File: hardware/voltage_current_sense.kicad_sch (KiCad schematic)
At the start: 36 parts, among them U10 NME0505SC, U11 LM324, U6 INA126U/2K5, U8 LTC6992CS6-2-TRMPBF, U9 6N137

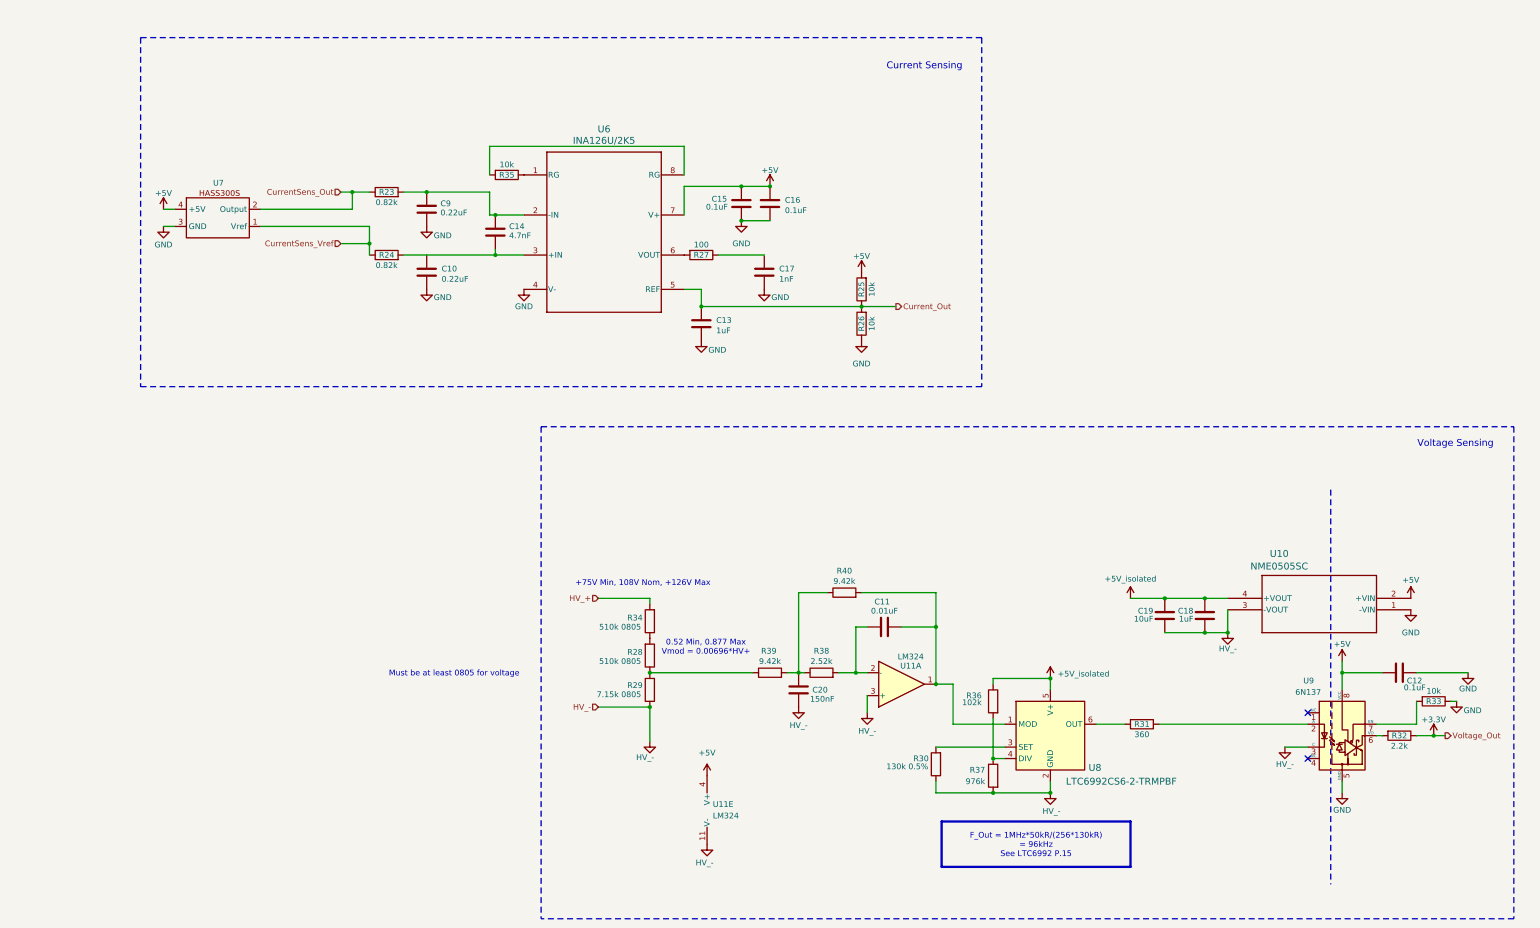
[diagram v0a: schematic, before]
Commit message: changes to sensing and footprints added
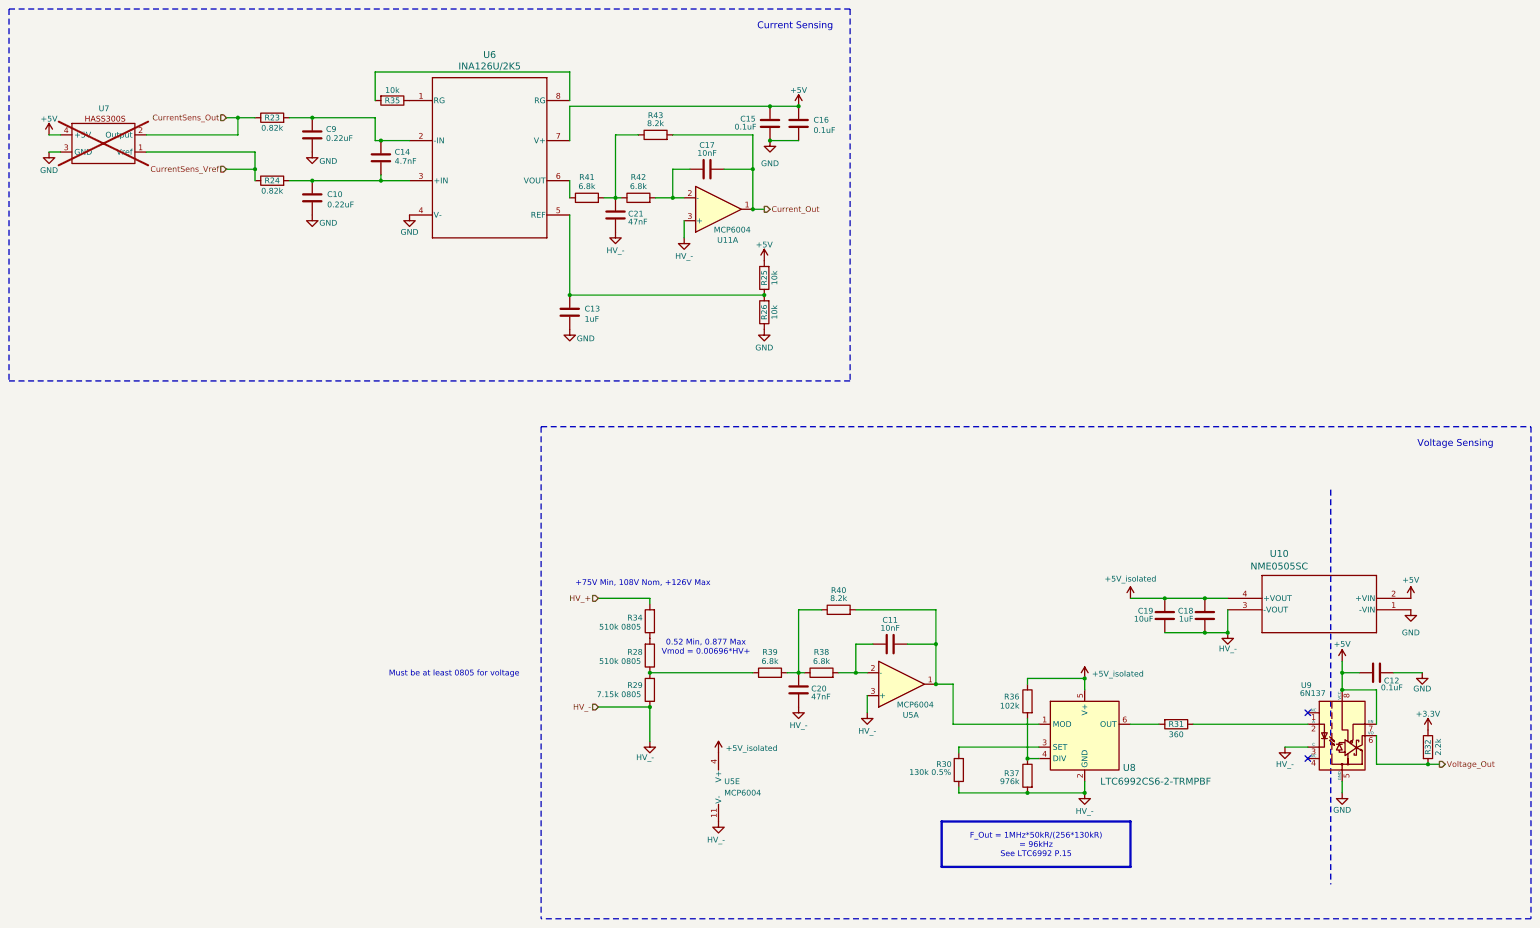
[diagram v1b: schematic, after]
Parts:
- removed R27: 100, symbol Device:R
- removed R33: 10k, symbol Device:R
- removed U11: LM324, symbol Amplifier_Operational:LM324
- added C21: 47nF, Capacitor_SMD:C_0805_2012Metric_Pad1.18x1.45mm_HandSolder, symbol Device:C
- added R41, R42: 6.8k, Resistor_SMD:R_0805_2012Metric_Pad1.20x1.40mm_HandSolder, symbol Device:R
- added R43: 8.2k, Resistor_SMD:R_0805_2012Metric_Pad1.20x1.40mm_HandSolder, symbol Device:R
- added U11, U5: MCP6004, Package_SO:SOIC-14_3.9x8.7mm_P1.27mm, symbol Amplifier_Operational:MCP6004
- C10, C12, C13, C14, C15, C16, C18, C19, C9: footprint (none) -> Capacitor_SMD:C_0805_2012Metric_Pad1.18x1.45mm_HandSolder
- C11: value 0.01uF -> 10nF; footprint (none) -> Capacitor_SMD:C_0805_2012Metric_Pad1.18x1.45mm_HandSolder
- C17: value 1nF -> 10nF; footprint (none) -> Capacitor_SMD:C_0805_2012Metric_Pad1.18x1.45mm_HandSolder
- C20: value 150nF -> 47nF; footprint (none) -> Capacitor_SMD:C_0805_2012Metric_Pad1.18x1.45mm_HandSolder
- R23, R24, R25, R26, R28, R29, R30, R31, R32, R34, R35, R36, R37: footprint (none) -> Resistor_SMD:R_0805_2012Metric_Pad1.20x1.40mm_HandSolder
- R38: value 2.52k -> 6.8k; footprint (none) -> Resistor_SMD:R_0805_2012Metric_Pad1.20x1.40mm_HandSolder
- R39: value 9.42k -> 6.8k; footprint (none) -> Resistor_SMD:R_0805_2012Metric_Pad1.20x1.40mm_HandSolder
- R40: value 9.42k -> 8.2k; footprint (none) -> Resistor_SMD:R_0805_2012Metric_Pad1.20x1.40mm_HandSolder
- U6: footprint D0008A_N -> Package_SO:SOIC-8_5.3x6.2mm_P1.27mm
- U7: now not fitted
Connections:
- net +5V: now also U9.7 (EN)
- net +5V_isolated: now also U5.4 (V+)
- net Current_Out: now also C17.2, R43.2, U11.1; no longer C13.1, R25.1, R26.2, U6.5 (REF)
- net GND: no longer C17.2
- net HV_-: now also C21.1, U11.3 (+), U5.11 (V-), U5.3 (+)
- net at C11.2, R40.2, U8.1 (MOD): now also U5.1
- net at C17.1: now also R42.2, U11.2 (-)
- net Voltage_Out: now reaches R32.2, U9.6 (VO)
- net at U6.6 (VOUT): now also R41.1
- net at C11.1, R38.2: now also U5.2 (-)
- new net: C21.2, R41.2, R42.1, R43.1
- new net: C13.1, R25.1, R26.2, U6.5 (REF)
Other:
- moved on the sheet: C10, C11, C12, C13, C14, C15, C16, C9, R23, R24, R25, R26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

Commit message: completed main board schematic
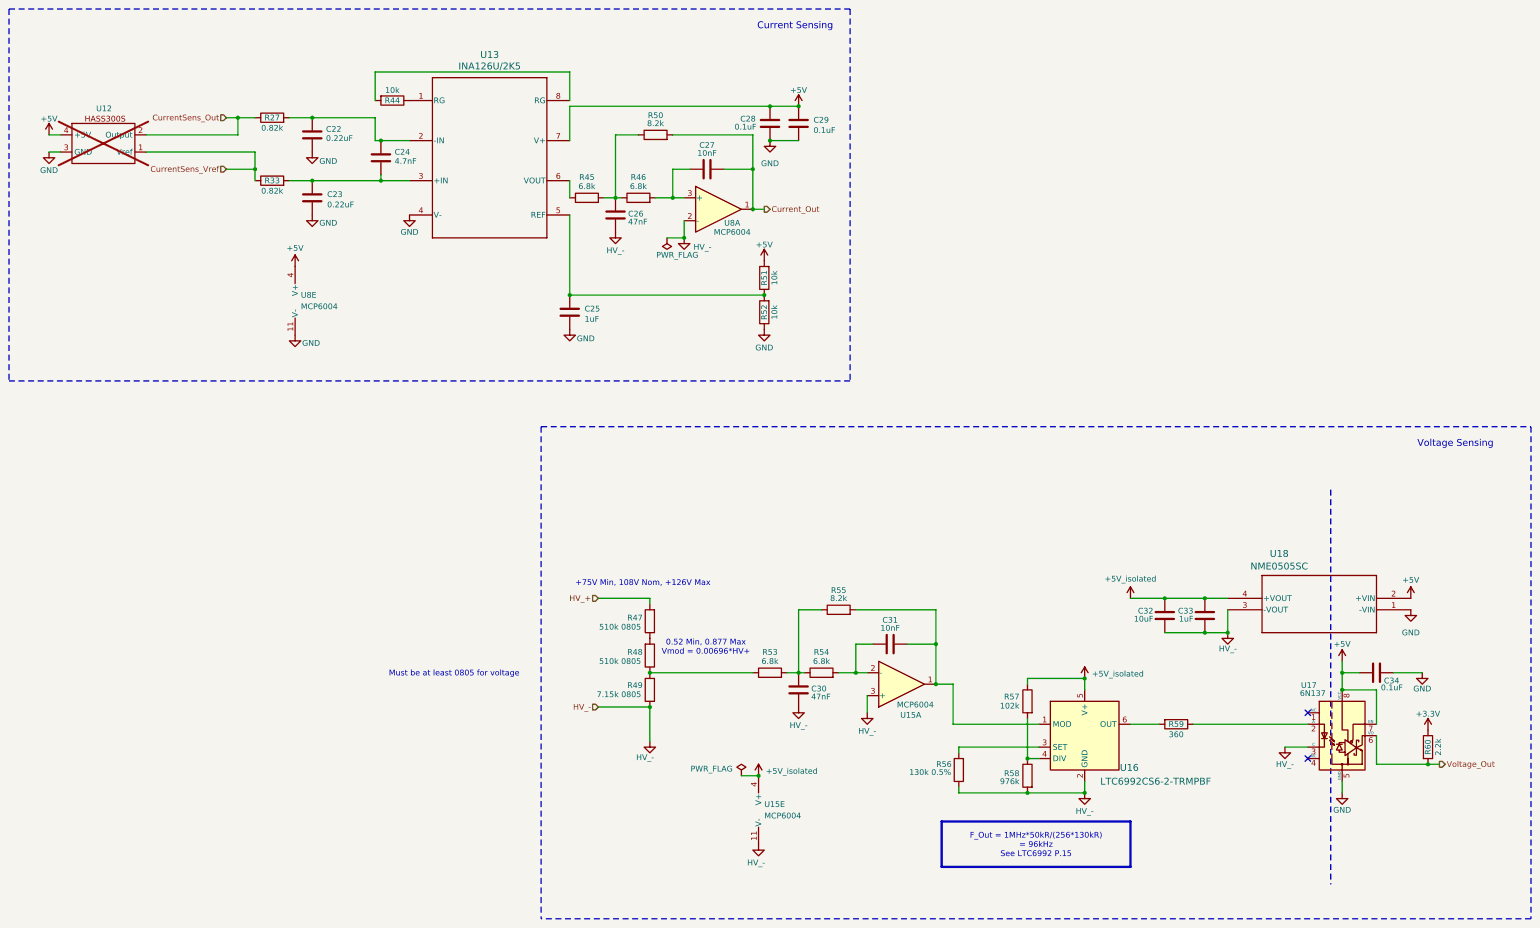
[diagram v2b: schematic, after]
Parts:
- removed U11: MCP6004, Package_SO:SOIC-14_3.9x8.7mm_P1.27mm, symbol Amplifier_Operational:MCP6004
- added U8: MCP6004, symbol Amplifier_Operational:MCP6004
- renumbered C9 to C22, C10 to C23, C14 to C24, C13 to C25, C21 to C26, C17 to C27, C15 to C28, C16 to C29, C20 to C30, C11 to C31, C19 to C32, C18 to C33, C12 to C34, R23 to R27, R24 to R33, R35 to R44, R41 to R45, R42 to R46, R34 to R47, R28 to R48, R29 to R49, R43 to R50, R25 to R51, R26 to R52, R39 to R53, R38 to R54, R40 to R55, R30 to R56, R36 to R57, R37 to R58, R31 to R59, R32 to R60, U7 to U12, U6 to U13, U5 to U15, U8 to U16, U9 to U17, U10 to U18
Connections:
- net +5V: now also U8.4 (V+)
- net Current_Out: now also U8.1
- net GND: now also U8.11 (V-)
- net HV_-: now also U8.2 (-)
- net at C27.1, R46.2: now also U8.3 (+)
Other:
- moved on the sheet: U15E
